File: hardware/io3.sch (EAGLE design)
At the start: 37 parts, among them IC2 74HC14D, IC3 74HC74D, Q1 BC857BSMD, U1 TXB0108PWR

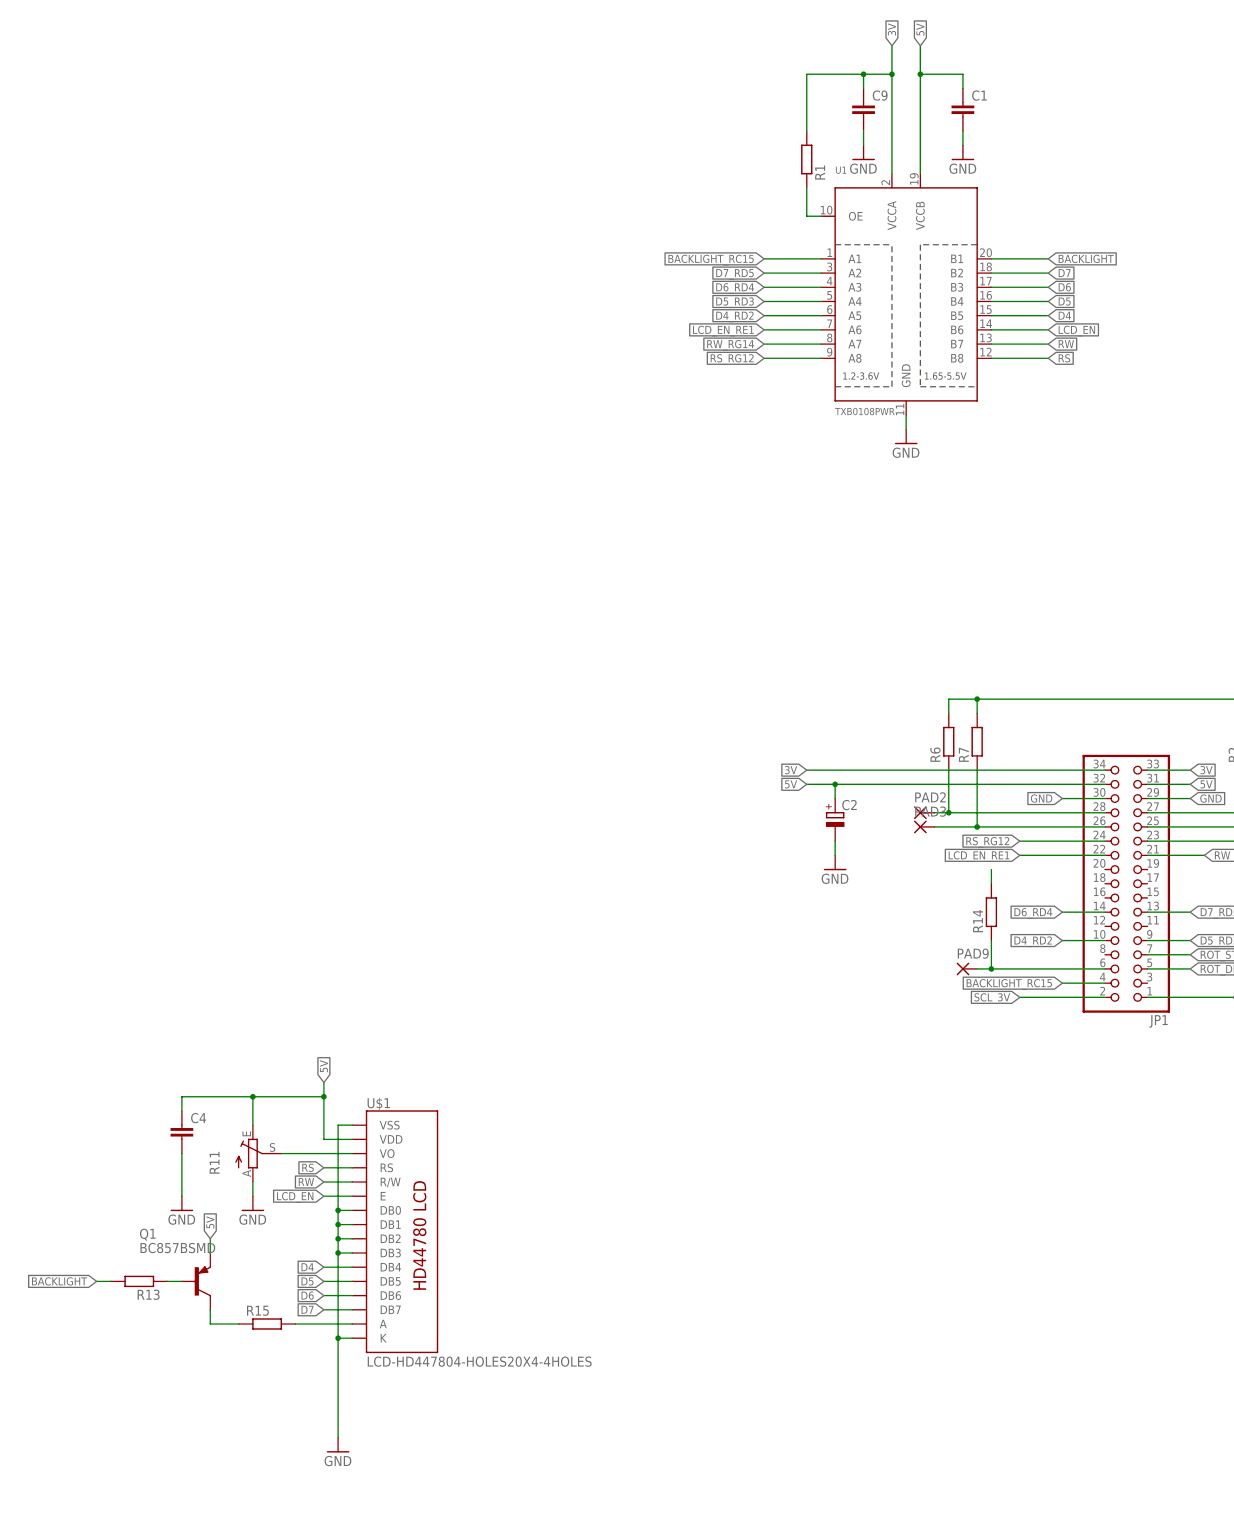
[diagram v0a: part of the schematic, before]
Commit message: IO PCB updated - no buffer
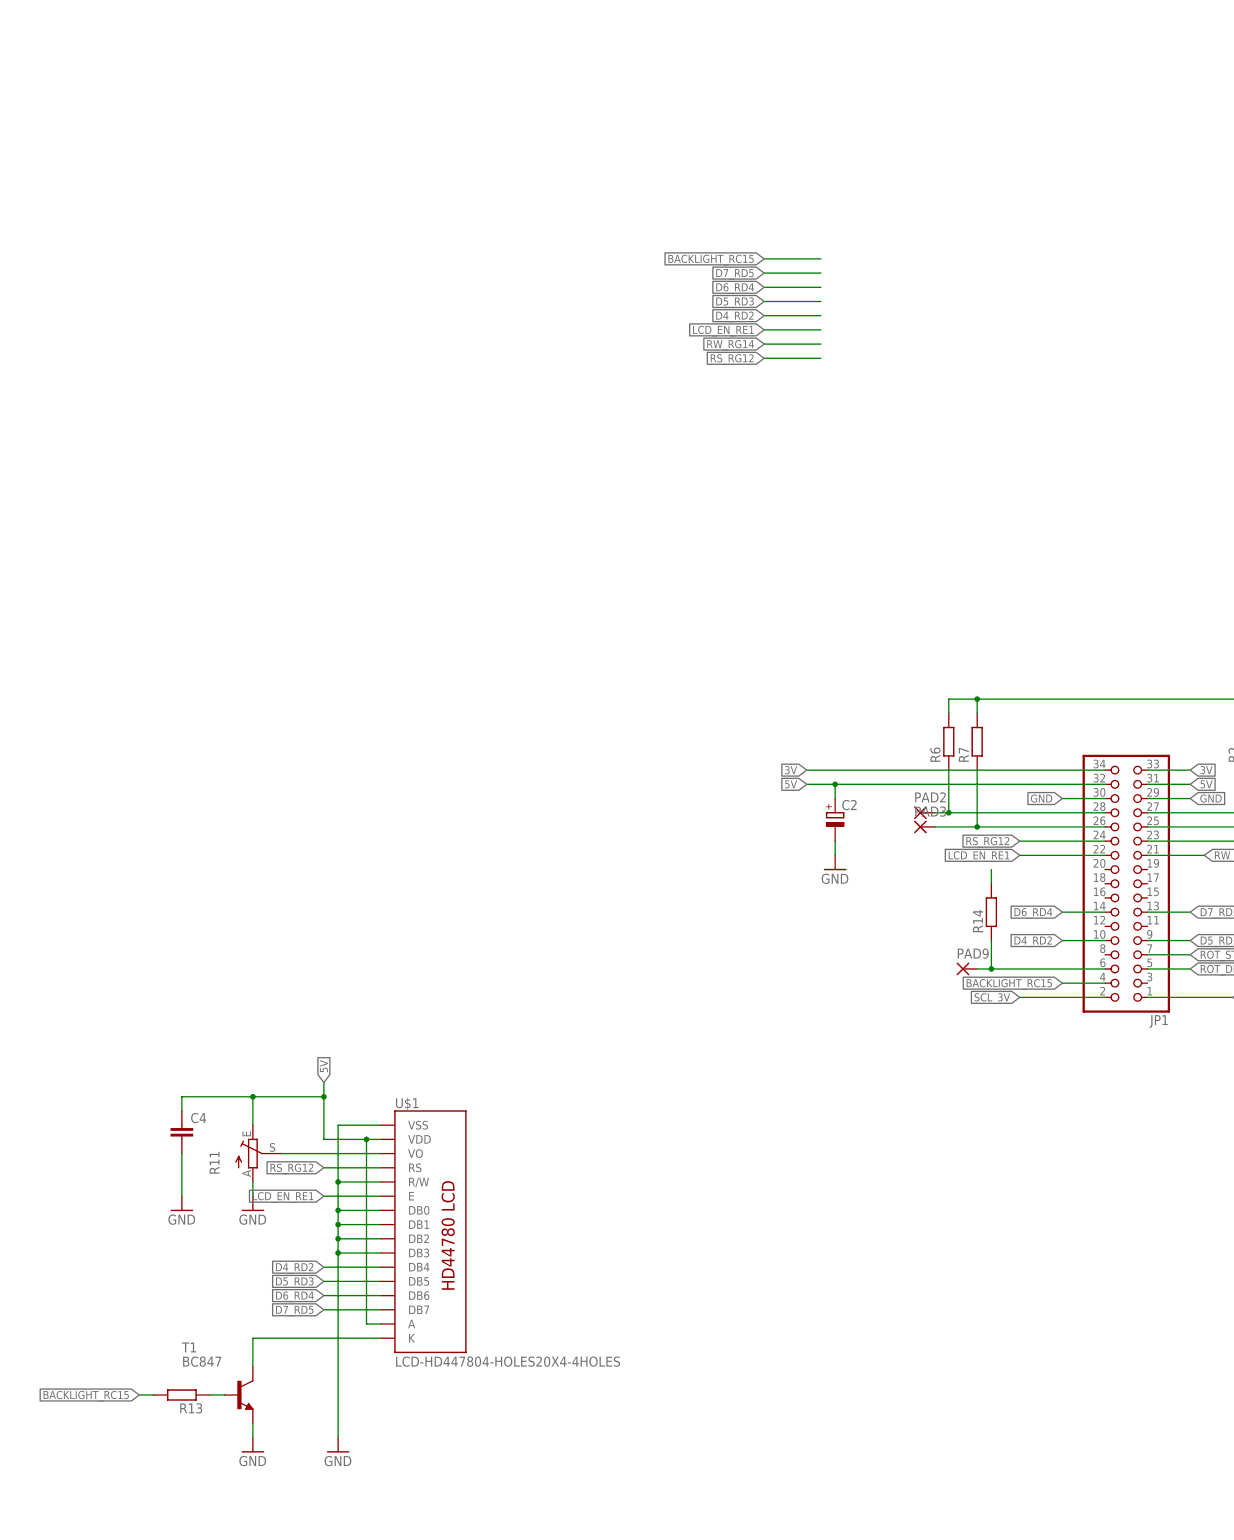
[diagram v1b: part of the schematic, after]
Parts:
- removed C1, C9: (no value), rcl:C-EUC0603
- removed Q1: BC857BSMD, transistor-pnp:BC857BSMD
- removed R1: (no value), rcl:R-EU_R0603
- removed R15: (no value), rcl:R-EU_R1206
- removed U1: TXB0108PWR, microbuilder:TXB0108PWR
- added T1: BC847, transistor:BC847
- R13: device rcl:R-EU_R0603 -> rcl:R-EU_0204/5
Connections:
- removed net BACKLIGHT: R13.2, U1.B1
- removed net D4: U$1.DB4, U1.B5
- removed net D5: U$1.DB5, U1.B4
- removed net D6: U$1.DB6, U1.B3
- removed net D7: U$1.DB7, U1.B2
- removed net LCD_EN: U$1.E, U1.B6
- removed net N$3: R15.2, U$1.A
- removed net N$4: R1.1, U1.OE
- removed net RS: U$1.RS, U1.B8
- removed net RW: U$1.R/W, U1.B7
- net 3V: no longer C9.1, R1.2, U1.VCCA
- net 5V: now also U$1.A; no longer C1.1, Q1.E, U1.VCCB
- net BACKLIGHT_RC15: now also R13.2; no longer U1.A1
- net D4_RD2: now also U$1.DB4; no longer U1.A5
- net D5_RD3: now also U$1.DB5; no longer U1.A4
- net D6_RD4: now also U$1.DB6; no longer U1.A3
- net D7_RD5: now also U$1.DB7; no longer U1.A2
- net GND: now also T1.E, U$1.R/W; no longer C1.2, C9.2, U$1.K, U1.GND
- net LCD_EN_RE1: now also U$1.E; no longer U1.A6
- net N$1: now also T1.C, U$1.K; no longer Q1.C, R15.1
- net N$6: now also T1.B; no longer Q1.B
- net RS_RG12: now also U$1.RS; no longer U1.A8
- net RW_RG14: no longer U1.A7
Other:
- moved on the sheet: R13, U$1

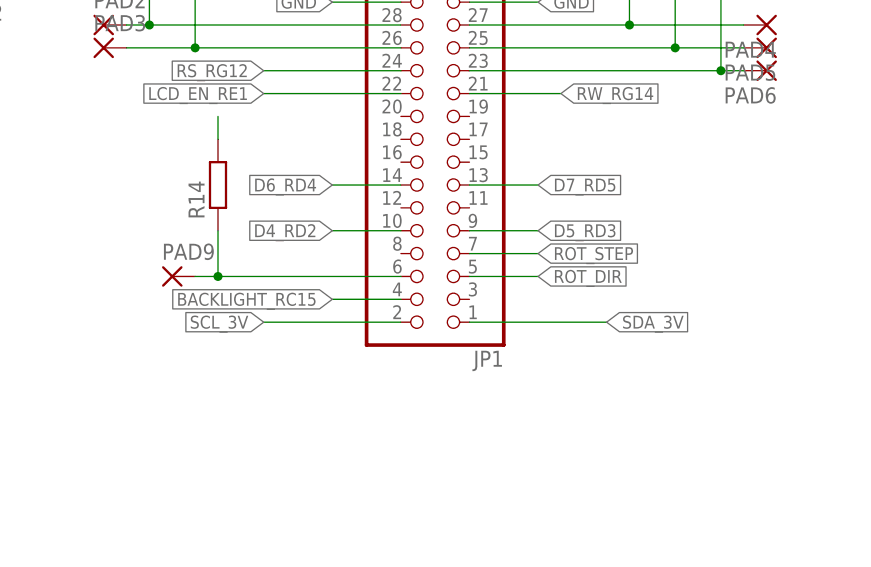
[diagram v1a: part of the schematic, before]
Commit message: Changes in PCB design allowing us to use bug free I2C1 instead of buggy I2C3
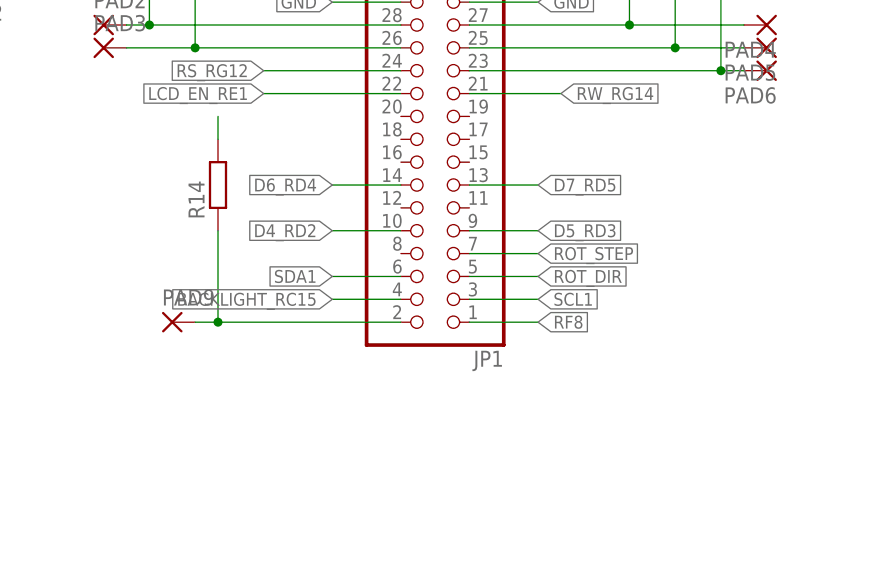
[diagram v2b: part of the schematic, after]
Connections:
- net SDA_3V renamed RF8
- removed net SCL_3V: JP1.2
- new net SCL1: JP1.3
- new net SDA1: JP1.6
- net ROT_SW: now also JP1.2; no longer JP1.6
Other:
- moved on the sheet: PAD9
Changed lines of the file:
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@@
 <instance part="PAD2" gate="1" x="144.78" y="195.58"/>
 <instance part="PAD3" gate="1" x="144.78" y="193.04"/>
-<instance part="PAD9" gate="1" x="152.4" y="167.64"/>
+<instance part="PAD9" gate="1" x="152.4" y="162.56"/>
 <instance part="C5" gate="G$1" x="279.4" y="251.46"/>
 <instance part="GND4" gate="1" x="279.4" y="241.3"/>
@@
 </segment>
 </net>
-<net name="SDA_3V" class="0">
-<segment>
-<wire x1="185.42" y1="162.56" x2="200.66" y2="162.56" width="0.1524" layer="91"/>
+<net name="RF8" class="0">
+<segment>
+<wire x1="185.42" y1="162.56" x2="193.04" y2="162.56" width="0.1524" layer="91"/>
 <pinref part="JP1" gate="A" pin="1"/>
-<label x="200.66" y="162.56" size="1.4224" layer="95" xref="yes"/>
-</segment>
-</net>
-<net name="SCL_3V" class="0">
-<segment>
-<wire x1="177.8" y1="162.56" x2="162.56" y2="162.56" width="0.1524" layer="91"/>
-<label x="162.56" y="162.56" size="1.4224" layer="95" rot="R180" xref="yes"/>
-<pinref part="JP1" gate="A" pin="2"/>
+<label x="193.04" y="162.56" size="1.4224" layer="95" xref="yes"/>
 </segment>
 </net>
@@
 <net name="ROT_SW" class="0">
 <segment>
-<pinref part="JP1" gate="A" pin="6"/>
-<wire x1="177.8" y1="167.64" x2="157.48" y2="167.64" width="0.1524" layer="91"/>
 <pinref part="R14" gate="G$1" pin="1"/>
-<wire x1="157.48" y1="167.64" x2="154.94" y2="167.64" width="0.1524" layer="91"/>
-<wire x1="157.48" y1="172.72" x2="157.48" y2="167.64" width="0.1524" layer="91"/>
-<junction x="157.48" y="167.64"/>
+<wire x1="157.48" y1="162.56" x2="154.94" y2="162.56" width="0.1524" layer="91"/>
+<wire x1="157.48" y1="172.72" x2="157.48" y2="162.56" width="0.1524" layer="91"/>
 <pinref part="PAD9" gate="1" pin="P"/>
+<pinref part="JP1" gate="A" pin="2"/>
+<wire x1="157.48" y1="162.56" x2="177.8" y2="162.56" width="0.1524" layer="91"/>
+<junction x="157.48" y="162.56"/>
 </segment>
 </net>
@@
 </segment>
 </net>
+<net name="SCL1" class="0">
+<segment>
+<pinref part="JP1" gate="A" pin="3"/>
+<wire x1="185.42" y1="165.1" x2="193.04" y2="165.1" width="0.1524" layer="91"/>
+<label x="193.04" y="165.1" size="1.4224" layer="95" xref="yes"/>
+</segment>
+</net>
+<net name="SDA1" class="0">
+<segment>
+<pinref part="JP1" gate="A" pin="6"/>
+<wire x1="177.8" y1="167.64" x2="170.18" y2="167.64" width="0.1524" layer="91"/>
+<label x="170.18" y="167.64" size="1.4224" layer="95" rot="R180" xref="yes"/>
+</segment>
+</net>
